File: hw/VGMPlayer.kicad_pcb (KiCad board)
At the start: 4 copper layers, 40 x 67 mm, 96 parts, among them J1 Micro_SD_Card, J2 EarPiece, M1 Mechanical-NC, P1 USB_C_Receptacle_16P, P2 SWD, P3 BATT, P5 ICSP, P6 CODEC, Q1 AO3401A, Q2 AO3401A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

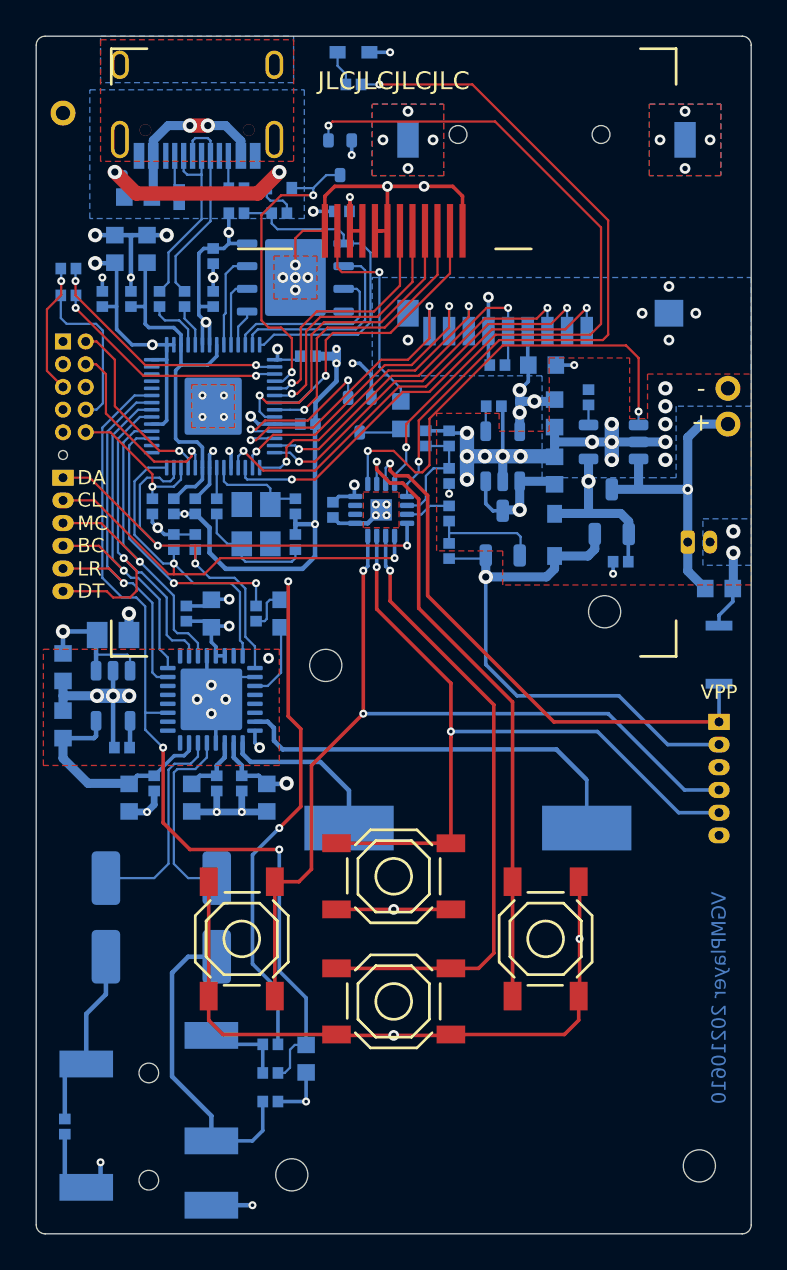
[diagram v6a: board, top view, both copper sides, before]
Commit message: Change 2N7002 footprint to SOT-523
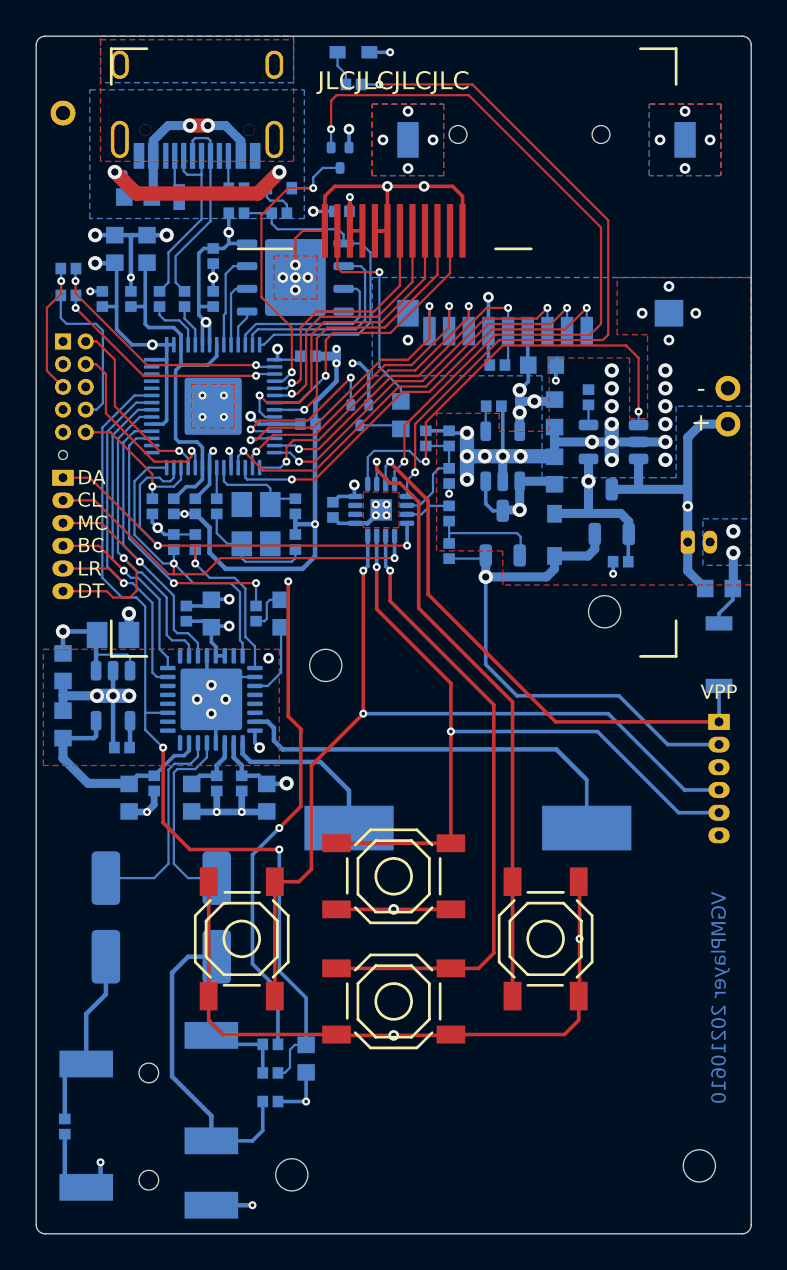
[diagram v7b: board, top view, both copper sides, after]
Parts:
- Q3, Q4: footprint BZ_Standard_IC:SOT-323-3 -> BZ_Standard_IC:SOT-523
- turned Q3 to 270 degrees
- turned Q4 to 270 degrees
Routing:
- net Net-(Q3-Pad1): track 40.9 -> 43.2 mm
- net Net-(U5-Pad1): track 26.0 -> 25.1 mm
- net /LCD_BL: track 9.15 -> 9.68 mm
- net GND: vias 83 -> 87

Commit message: Fix SWD connector orientation
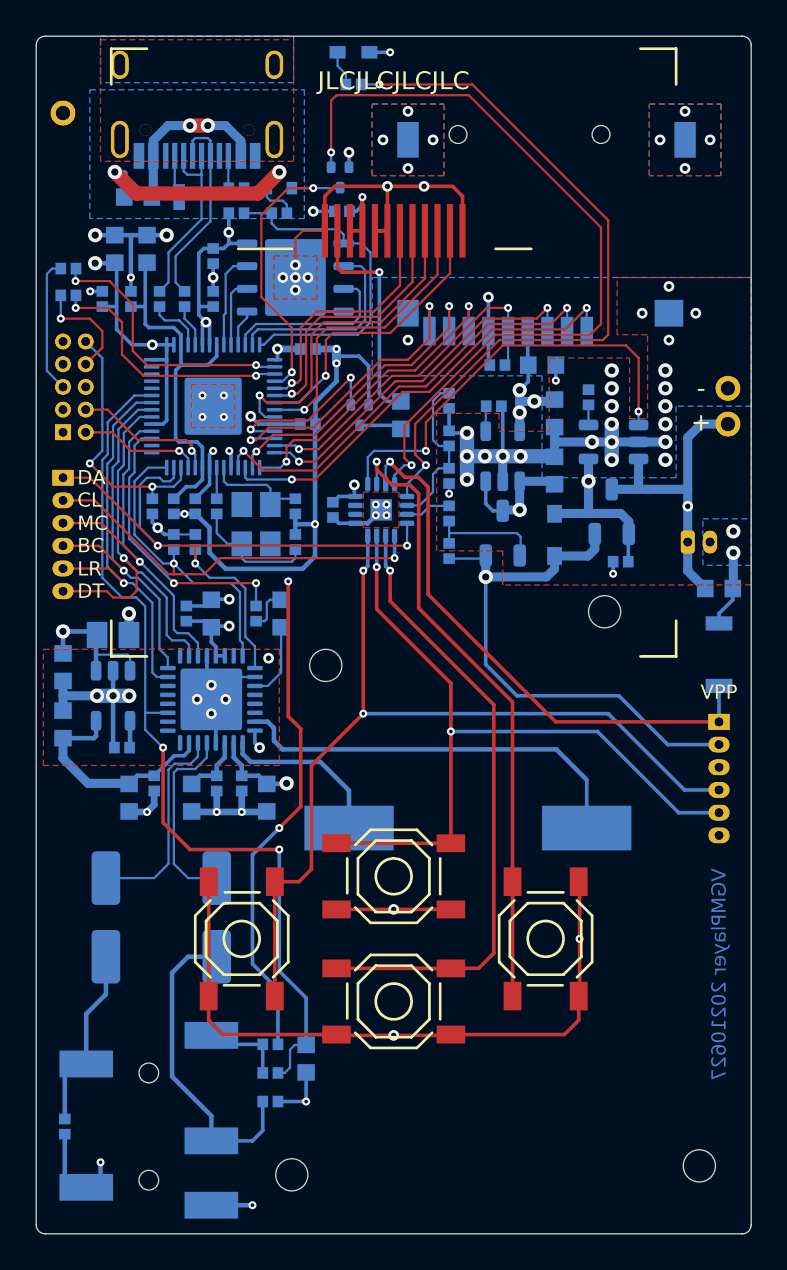
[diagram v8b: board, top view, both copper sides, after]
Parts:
- removed M1: Mechanical-NC, BZ_Mechanical:Hole-Mech_0.5
- moved P2 5.08 mm to (131.5, 99.2), turned to 90 degrees
- moved C36 2.47 mm to (153.1, 97.4), turned to 270 degrees
- moved Q3 1.10 mm to (147.0, 84.9)
- moved C13 0.40 mm to (145.2, 94.5)
- renumbered TP3 to TP2, TP2 to TP3
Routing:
- net /RUN: track 8.60 -> 14.7 mm, vias 1 -> 2
- net /SWDIO: track 10.5 -> 6.85 mm
- net Net-(C36-Pad1): track 6.30 -> 9.31 mm
- net Net-(P2-Pad8): track 9.09 -> 6.15 mm, vias 0 -> 1
- net /SWCLK: track 10.9 -> 8.08 mm
- net 3V3: track 133.7 -> 131.8 mm
- net Net-(Q3-Pad1): track 43.2 -> 44.8 mm
- net GND: track 198.6 -> 199.7 mm, vias 87 -> 86
- net /TX: track 14.1 -> 15.3 mm
- net /RX: track 13.5 -> 14.5 mm
- net Net-(U5-Pad1): track 25.1 -> 24.2 mm
- net /BOOT: track 17.8 -> 16.9 mm
- net Net-(P2-Pad5): track 7.23 -> 7.63 mm, vias 1 -> 0
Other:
- board text added: "VGMPlayer 20210627"
- board text removed: "VGMPlayer 20210610"
